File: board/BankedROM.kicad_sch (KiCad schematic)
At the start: 16 parts, among them U26 SST39SF040, U27 SST39SF040, U28 SST39SF040, U29 SST39SF040, U30 SST39SF040, U31 SST39SF040, U32 SST39SF040, U33 SST39SF040

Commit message: V2.0 rev 2.0D: clock stretching, OS ROM paging and review fixes
Bus timing:
- New GAL C (U88) generates PHI2/PHI1 and the 3.58 MHz sound clock from
  the 14.318 MHz master, replacing the U35 74F191 divider. J36 now selects
  7.16 or 3.58 MHz.
- Banked RAM, banked ROM and slot I/O ($FF20-$FFEF) get one extra PHI2-low
  period plus 0-3 extra PHI2-high periods set in $FFF5 (GAL D). This
  replaces the on-board RDY wait generator; cards can still pull RDY.
- Write strobes are now hold-time safe: PHI1 comes straight from GAL C
  and RWB_M straight from GAL B2.

Review fixes:
- OS ROM chip enable from a single-level decode, output enable from
  GAL B1; -55 part specified. Full 4K OS ROM paging via GAL G.
- Vector RAM writes only during PHI2; $FFF0-$FFFF no longer slowed.
- YM2151 /WR on RWB_M. U62 removed. RB0-RB7 pull-ups (RN5).
- Slot clocks driven through U56 and U34 with 33R series resistors.
- J38 enables in-system flashing of the banked ROMs.
- W65C22S/W65C51N, AS6C4008, DS1813-5 and CY7C192-25 values; R4 1k.
- J7 pin 8 no longer +5V; +5VA renamed +5VSB; serial handshake loop.
- Sheet titles and revisions, slot symbol pin fixes, and project symbol
  and footprint libraries so the project opens on another machine.

Co-Authored-By: Claude Opus 5.5 <noreply@anthropic.com>
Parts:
- added J38: FLASH WE, Connector_PinHeader_2.54mm:PinHeader_1x02_P2.54mm_Vertical, symbol Connector_Generic:Conn_01x02
- added R25: 10k, Resistor_THT:R_Axial_DIN0204_L3.6mm_D1.6mm_P5.08mm_Horizontal, symbol Device:R
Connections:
- net +5V: now also R25.1; no longer U26.31 (PGM), U27.31 (PGM), U28.31 (PGM), U29.31 (PGM), U30.31 (PGM), U31.31 (PGM), U32.31 (PGM), U33.31 (PGM)
- new net RWB_M: J38.2 (Pin_2)
- new net nFLASH_WE: J38.1 (Pin_1), R25.2, U26.31 (PGM), U27.31 (PGM), U28.31 (PGM), U29.31 (PGM), U30.31 (PGM), U31.31 (PGM), U32.31 (PGM), U33.31 (PGM)
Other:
- title: ZeroPage $00/$01 Mirror Memory and RAM/ROM Bank Logic -> Banked ROM ($A000-$DFFF)

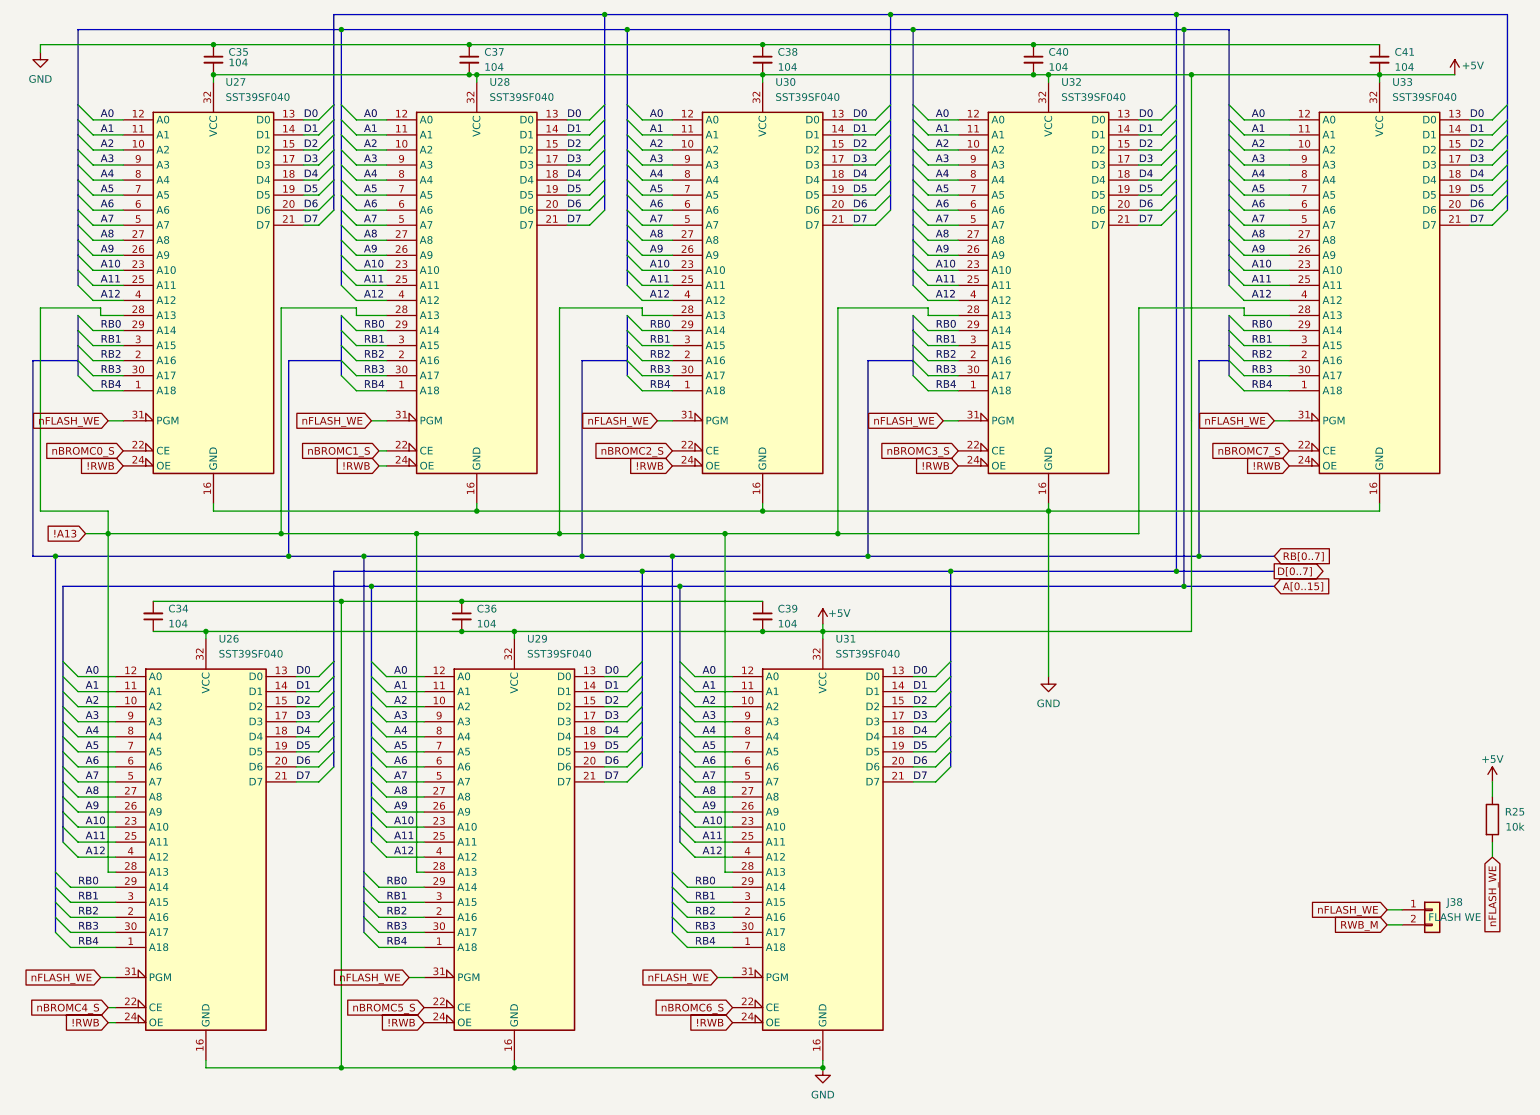
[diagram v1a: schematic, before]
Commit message: V2.0: split Support sheet, add stereo amplifier and on-board speakers
Support sheet reorganized (connectivity unchanged):
- Support.kicad_sch renamed to Power: ATX, front panel, reset, soft power, -5V
- Oscillators and their parts moved to Clocks (now US Ledger)
- Sound-chip decoupling and line-out parts moved to Sound
- VIA CB1/CB2/SPI pull-ups moved to Connectors
- Also includes minor schematic edits made before the reorganization

Audio output rework (Sound, now A3):
- U89 TDA2822M stereo amplifier on 9 V from U90 L7809 (fed by +12V)
- RV1 dual 10k log volume pot behind R26/R27 220k attenuators
- J18 moved from Connectors and now uses the switched TRS symbol:
  a plug lifts T/R off TN/RN and mutes the on-board speakers
- LS1/LS2 8 ohm mini speakers through R30/R31 (15R 0.5 W)
- New footprint Speaker_D32mm_P15.24mm_P17.50mm (two pad pairs, fits
  Adafruit 1898 or Kitronik 3316)
- J39 line-out header (LINE_L, LINE_R, GNDA)
- R18 stays the single GNDA-GND tie, to sit at U89 pin 4
- TDA2822M symbol added to hydra16.kicad_sym

Co-Authored-By: Claude Opus 5.5 <noreply@anthropic.com>
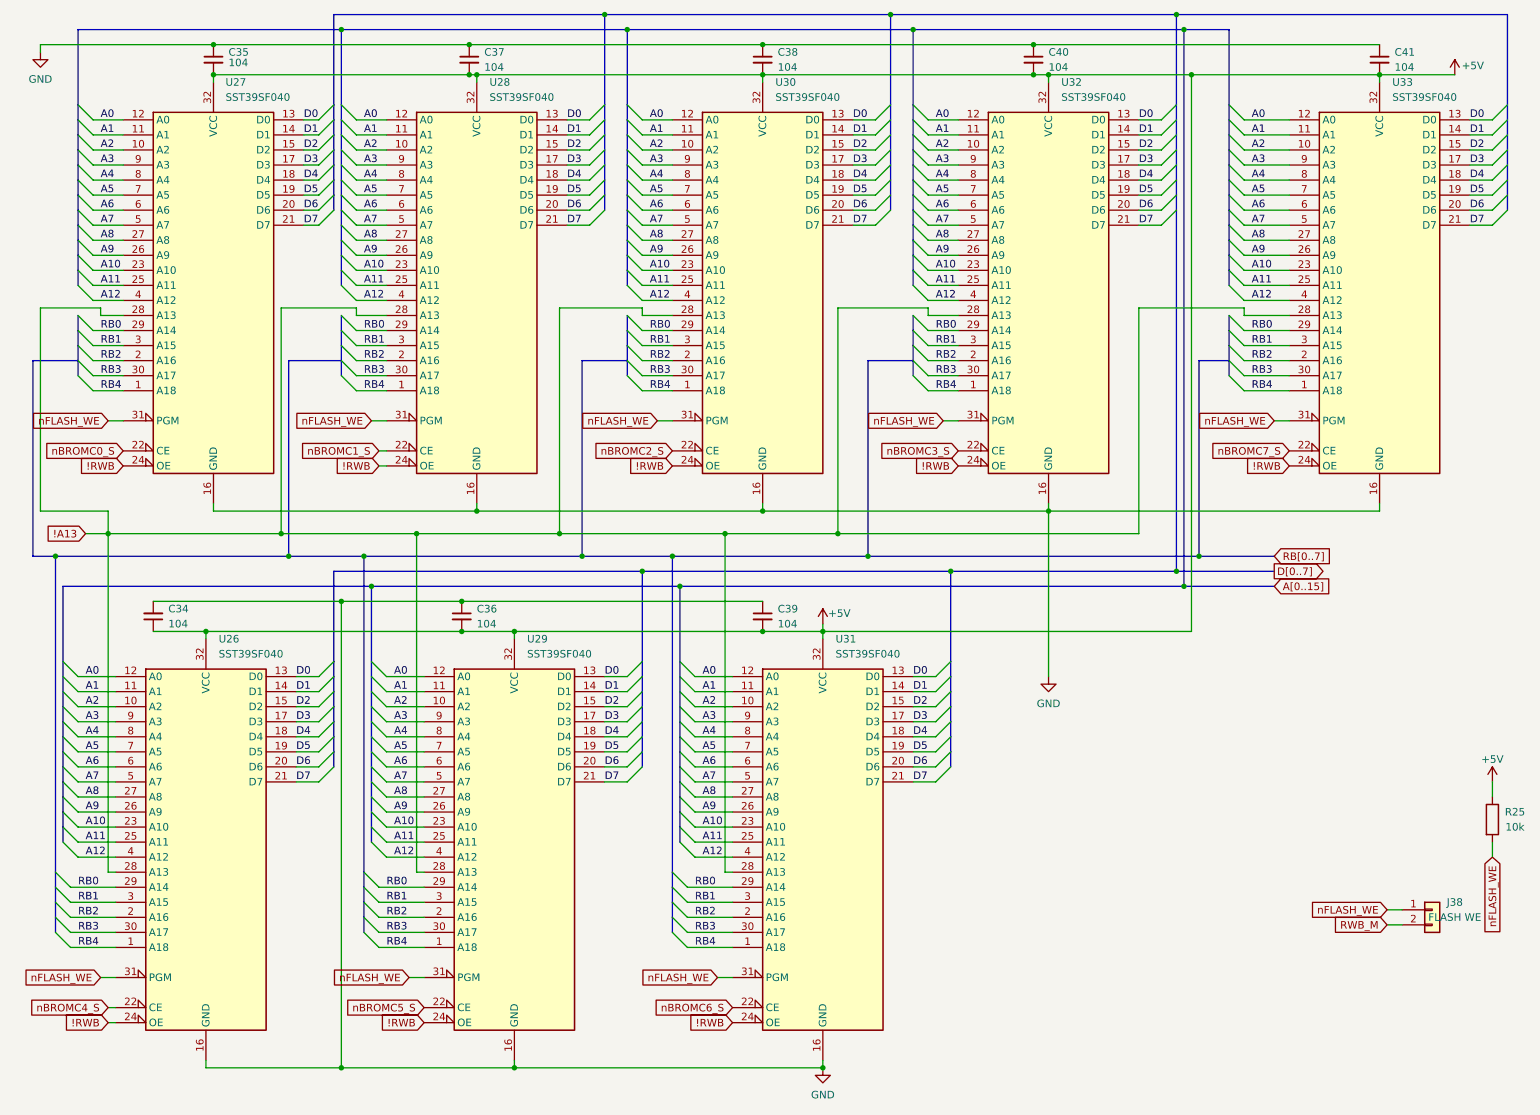
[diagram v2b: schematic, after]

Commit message: V2.0: speaker headers, A/D bus fix, layout edits
- On-board speakers LS1/LS2 replaced by 2-pin headers J40 (SPEAKER L)
  and J41 (SPEAKER R) for external mini speakers: pin 1 speaker
  (through R30/R31), pin 2 GNDA; J18 still mutes them
- Connectors: a layout move had joined the A[0..15] and D[0..7] buses
  at two crossings (shorting A0-A7 to D0-D7); buses separated again,
  connectivity matches the previous commit
- Layout edits across the sheets (no other connectivity change)
- PCB updated from the schematic

Co-Authored-By: Claude Opus 5.5 <noreply@anthropic.com>
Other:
- title: Banked ROM ($A000-$DFFF) -> Expansion Slots, SPI Headers and Port A
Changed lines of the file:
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@@
 	(paper "USLetter")
 	(title_block
-		(title "Banked ROM ($A000-$DFFF)")
+		(title "Expansion Slots, SPI Headers and Port A")
 		(date "2026-10-06")
 		(rev "2.0D")
